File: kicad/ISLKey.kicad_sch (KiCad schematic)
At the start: 13 parts, among them J1 Exit Button N/O, J2 Door Contact N/C, J4 Tamper N/C, J5 Fire volt-free N/C (series, o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, K1 2-Ch Relay Module, U1 ISLKey Controller (TTGO), U2 PC817 fire-link monitor -> GP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

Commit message: kicad: rebuild ISLKey TTGO carrier as a real, manufacturable design
Replace the box-symbol connectivity sketch with a proper KiCad 10 design
generated from gen/ scripts that embed genuine library symbols (correct
pin<->pad maps) with footprints assigned:

- Schematic (ISLKey.kicad_sch): 40 parts, ERC 0/0. TTGO T-Display carrier
  with dual onboard SANYOU-SRD relays (2N2222 drivers, flyback, green status
  LED across each coil), monitored fire link (PC817 + COM<->fire jumper),
  wide-input isolated PSU (5-60V AC/DC -> KBU bridge + fuse -> isolated 12V
  DC-DC module -> 12->5V buck), 12V lock/aux output, and 18650 battery
  passthrough. PGND/GND kept separate to preserve isolation.
- PCB (ISLKey.kicad_pcb): all 40 footprints placed + nets assigned via
  pcbnew, board outline + 4x M3 holes, DRC 0 (only unrouted ratsnest).
- BOM (ISLKey-BOM.csv): 30 grouped line items, all real footprints.
- Generators: gen/kicad_lib.py, gen/make_schematic.py, gen/make_pcb.py.

Co-Authored-By: Claude Opus 4.8 <noreply@anthropic.com>
Claude-Session: https://claude.ai/code/session_01WaJbCVpNNC7xF4fkqWpjpA
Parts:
- removed BT1: 2x18650 UPS 5V, symbol islkey:UPS_18650
- removed D1: 1N4007 flyback, symbol islkey:Diode_1N4007
- removed J1: Exit Button N/O, symbol islkey:Conn_Exit
- removed J2: Door Contact N/C, symbol islkey:Conn_Door
- removed J4: Tamper N/C, symbol islkey:Conn_Tamper
- removed J5: Fire volt-free N/C (series, opens on fire), symbol islkey:Fire_Contact
- removed K1: 2-Ch Relay Module, symbol islkey:Relay_2Ch
- removed LK1: Electric Strike / Maglock 12V, symbol islkey:Lock
- removed PS1: 5V Mains PSU, symbol islkey:Mains_PSU
- removed PS2: 12V Lock PSU, symbol islkey:Lock_PSU
- removed R1: 2k2 opto LED series, symbol islkey:R_Opto
- removed U1: ISLKey Controller (TTGO), symbol islkey:ESP32_TTGO
- removed U2: PC817 fire-link monitor -> GPIO26, symbol islkey:Opto_PC817
- added BR1: KBU4M (4A), Diode_THT:Diode_Bridge_Vishay_KBU, symbol Diode_Bridge:KBU4A
- added C1: 100uF/16V, Capacitor_THT:CP_Radial_D6.3mm_P2.50mm, symbol Device:C_Polarized
- added C2, C3: 100nF, Capacitor_THT:C_Disc_D5.0mm_W2.5mm_P5.00mm, symbol Device:C
- added C4: 100uF/100V, Capacitor_THT:CP_Radial_D6.3mm_P2.50mm, symbol Device:C_Polarized
- added C5: 100uF/25V, Capacitor_THT:CP_Radial_D6.3mm_P2.50mm, symbol Device:C_Polarized
- added D1, D2: 1N4007, Diode_THT:D_DO-41_SOD81_P10.16mm_Horizontal, symbol Device:D
- added D3: PWR, LED_THT:LED_D3.0mm, symbol Device:LED
- added D4, D5: GRN, LED_THT:LED_D3.0mm, symbol Device:LED
- added F1: T2A, Fuse:Fuseholder_Clip-5x20mm_Keystone_3512_Inline_P23.62x7.27mm_D1.02x1.57mm_Horizontal, symbol Device:Fuse
- added J1: TTGO Left, Connector_PinSocket_2.54mm:PinSocket_1x12_P2.54mm_Vertical, symbol Connector_Generic:Conn_01x12
- added J10: 5-60V AC/DC IN, TerminalBlock_Phoenix:TerminalBlock_Phoenix_MKDS-3-2-5.08_1x02_P5.08mm_Horizontal, symbol Connector:Screw_Terminal_01x02
- added J11: 12V OUT (lock/aux), TerminalBlock_Phoenix:TerminalBlock_Phoenix_MKDS-3-2-5.08_1x02_P5.08mm_Horizontal, symbol Connector:Screw_Terminal_01x02
- added J13: TTGO batt pads, Connector_PinHeader_2.54mm:PinHeader_1x02_P2.54mm_Vertical, symbol Connector_Generic:Conn_01x02
- added J14: 18650 pack, TerminalBlock_Phoenix:TerminalBlock_Phoenix_MKDS-1,5-2-5.08_1x02_P5.08mm_Horizontal, symbol Connector:Screw_Terminal_01x02
- added J2: TTGO Right, Connector_PinSocket_2.54mm:PinSocket_1x12_P2.54mm_Vertical, symbol Connector_Generic:Conn_01x12
- added J3: Exit btn, TerminalBlock_Phoenix:TerminalBlock_Phoenix_MKDS-1,5-2-5.08_1x02_P5.08mm_Horizontal, symbol Connector:Screw_Terminal_01x02
- added J4: Door contact, TerminalBlock_Phoenix:TerminalBlock_Phoenix_MKDS-1,5-2-5.08_1x02_P5.08mm_Horizontal, symbol Connector:Screw_Terminal_01x02
- added J5: Tamper, TerminalBlock_Phoenix:TerminalBlock_Phoenix_MKDS-1,5-2-5.08_1x02_P5.08mm_Horizontal, symbol Connector:Screw_Terminal_01x02
- added J6: LOCK COM/NO/NC, TerminalBlock_Phoenix:TerminalBlock_Phoenix_MKDS-1,5-3-5.08_1x03_P5.08mm_Horizontal, symbol Connector:Screw_Terminal_01x03
- added J7: AUX COM/NO/NC, TerminalBlock_Phoenix:TerminalBlock_Phoenix_MKDS-1,5-3-5.08_1x03_P5.08mm_Horizontal, symbol Connector:Screw_Terminal_01x03
- added J8: Fire volt-free, TerminalBlock_Phoenix:TerminalBlock_Phoenix_MKDS-1,5-2-5.08_1x02_P5.08mm_Horizontal, symbol Connector:Screw_Terminal_01x02
- added J9: Fire link COM-Fire, Connector_PinHeader_2.54mm:PinHeader_1x02_P2.54mm_Vertical, symbol Connector_Generic:Conn_01x02
- added K1, K2: SRD-05VDC-SL-C, Relay_THT:Relay_SPDT_SANYOU_SRD_Series_Form_C, symbol Relay:SANYOU_SRD_Form_C
- added Q1, Q2: PN2222A, Package_TO_SOT_THT:TO-92_Inline, symbol Transistor_BJT:Q_NPN_EBC
- added R1, R3, R6, R7, R8: 1k, Resistor_THT:R_Axial_DIN0207_L6.3mm_D2.5mm_P7.62mm_Horizontal, symbol Device:R
- added R2, R4: 10k, Resistor_THT:R_Axial_DIN0207_L6.3mm_D2.5mm_P7.62mm_Horizontal, symbol Device:R
- added R5: 2k2, Resistor_THT:R_Axial_DIN0207_L6.3mm_D2.5mm_P7.62mm_Horizontal, symbol Device:R
- added U1: PC817, Package_DIP:DIP-4_W7.62mm, symbol Isolator:PC817
- added U3: ISO DCDC ->12V (e.g. Mornsun URB), Connector_PinHeader_2.54mm:PinHeader_1x04_P2.54mm_Vertical, symbol Connector_Generic:Conn_01x04
- added U4: BUCK 12->5V (e.g. MP1584), Connector_PinHeader_2.54mm:PinHeader_1x03_P2.54mm_Vertical, symbol Connector_Generic:Conn_01x03
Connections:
- net +12V: now also C5.1, J11.1 (Pin_1), U3.4 (Pin_4), U4.1 (Pin_1)
- net +5V: now also C1.1, C2.1, D1.1 (K), D2.1 (K), D3.2 (A), D4.2 (A), D5.2 (A), J2.12 (Pin_12), K1.5, K2.5, U4.3 (Pin_3)
- net DOOR: now also J2.8 (Pin_8), J4.1 (Pin_1)
- net EXIT: now also J1.8 (Pin_8), J3.1 (Pin_1)
- net FIRE_A: now also J8.1 (Pin_1), J9.2 (Pin_2), R5.1
- net GND: now also C1.2, C2.2, C3.2, C5.2, J1.1 (Pin_1), J1.10 (Pin_10), J1.11 (Pin_11), J1.2 (Pin_2), J11.2 (Pin_2), J2.11 (Pin_11), J3.2 (Pin_2), J4.2 (Pin_2), J5.2 (Pin_2), Q1.1 (E), Q2.1 (E), R2.2, R4.2, R6.2, U1.3, U3.3 (Pin_3), U4.2 (Pin_2)
- net OPTO_A: now also R5.2, U1.1
- net TAMPER: now also J2.10 (Pin_10), J5.1 (Pin_1)
- new net +3V3: C3.1, J1.12 (Pin_12), J2.1 (Pin_1)
- new net ACIN1: BR1.2, F1.2
- new net ACL: F1.1, J10.1 (Pin_1)
- new net ACN: BR1.3, J10.2 (Pin_2)
- new net D3K: D3.1 (K), R6.1
- new net D4K: D4.1 (K), R7.1
- new net D5K: D5.1 (K), R8.1
- new net FIRE_B: J8.2 (Pin_2), U1.2
- new net FIRE_SENSE: J2.9 (Pin_9), U1.4
- new net GND_BAT: J13.2 (Pin_2), J14.2 (Pin_2)
- new net K1_C: D1.2 (A), K1.2, Q1.3 (C), R7.2
- new net K2_C: D2.2 (A), K2.2, Q2.3 (C), R8.2
- new net LK1_COM: J6.1 (Pin_1), J9.1 (Pin_1), K1.1
- new net LK1_NC: J6.3 (Pin_3), K1.4
- new net LK1_NO: J6.2 (Pin_2), K1.3
- new net LK2_COM: J7.1 (Pin_1), K2.1
- new net LK2_NC: J7.3 (Pin_3), K2.4
- new net LK2_NO: J7.2 (Pin_2), K2.3
- new net PGND: BR1.4 (-), C4.2, U3.2 (Pin_2)
- new net RAWP: BR1.1 (+), C4.1, U3.1 (Pin_1)
- new net RLY1: J2.6 (Pin_6), R1.1
- new net RLY1_B: Q1.2 (B), R1.2, R2.1
- new net RLY2: J2.7 (Pin_7), R3.1
- new net RLY2_B: Q2.2 (B), R3.2, R4.1
- new net VBAT: J13.1 (Pin_1), J14.1 (Pin_1)
- no-connect marks 0 -> 10
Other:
- title: ISLKey Door Controller — TTGO T-Display -> ISLKey TTGO Carrier Board

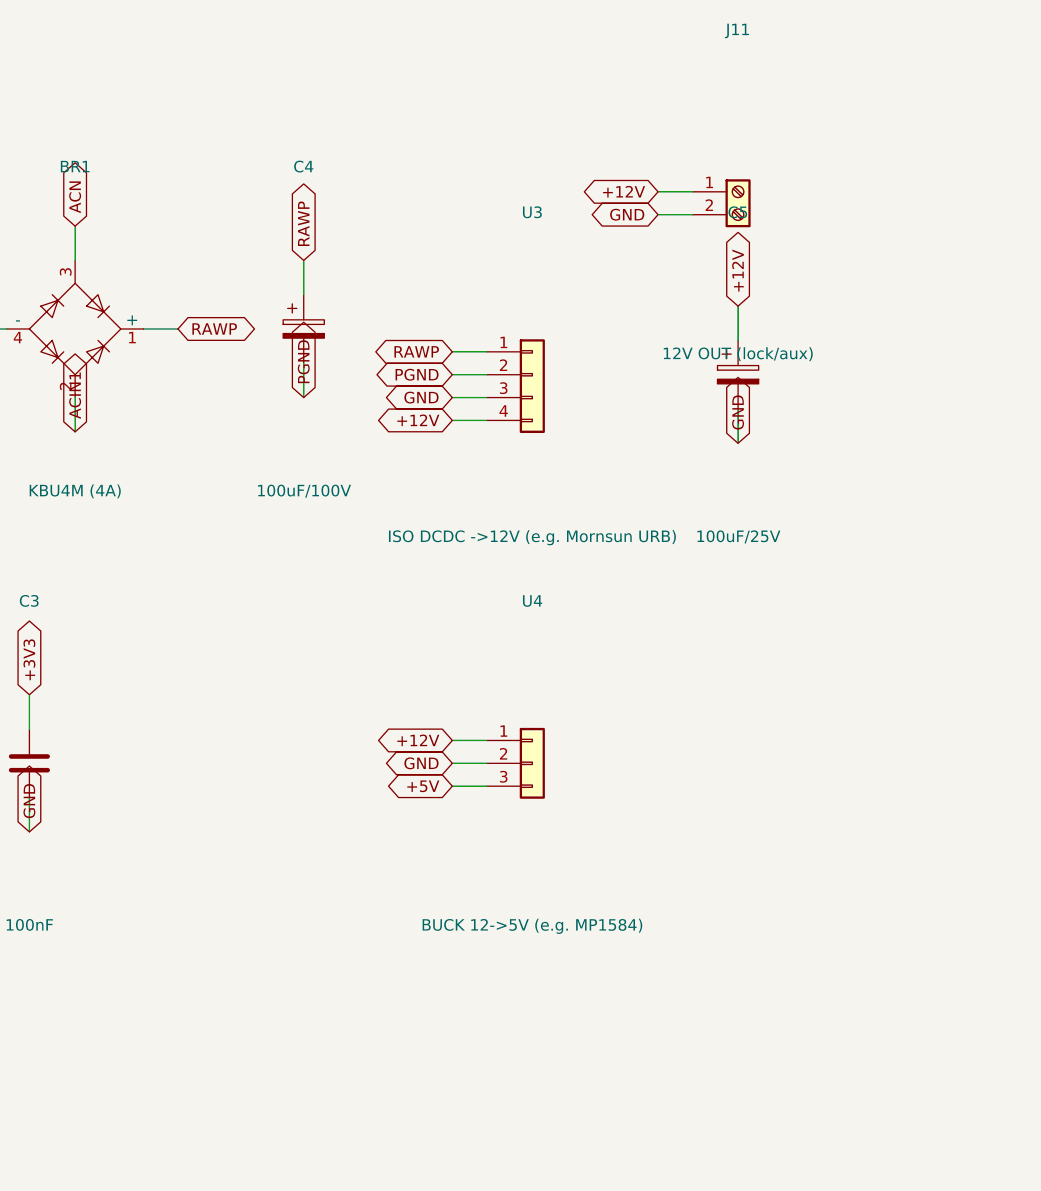
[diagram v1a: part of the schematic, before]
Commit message: kicad: use real Traco parts for the wide-input PSU
Replace the two generic module-header placeholders with genuine parts +
KiCad footprints:
- U3 isolated 12V: Traco TEN20-2412WIN (9-36V in -> isolated 12V/20W),
  footprint Converter_DCDC_TRACO_TEN20-xxxx_THT. Remote pin left open
  (positive logic, open = ON); Trim pin NC.
- U4 buck 12->5V for the TTGO: Traco TSR-1-2450 (SIP-3), footprint
  Converter_DCDC_TRACO_TSR-1_THT.
- Add PWR_FLAG on the raw primary rails (RAWP/PGND) so ERC sees them driven
  (bridge diode outputs are 'passive'); flags excluded from board + BOM.

ERC 0/0, DRC 0 (unrouted ratsnest only). One board covers 12/24V systems;
pin-compatible TEN20-4812WIN swaps in for 48V.

Co-Authored-By: Claude Opus 4.8 <noreply@anthropic.com>
Claude-Session: https://claude.ai/code/session_01WaJbCVpNNC7xF4fkqWpjpA
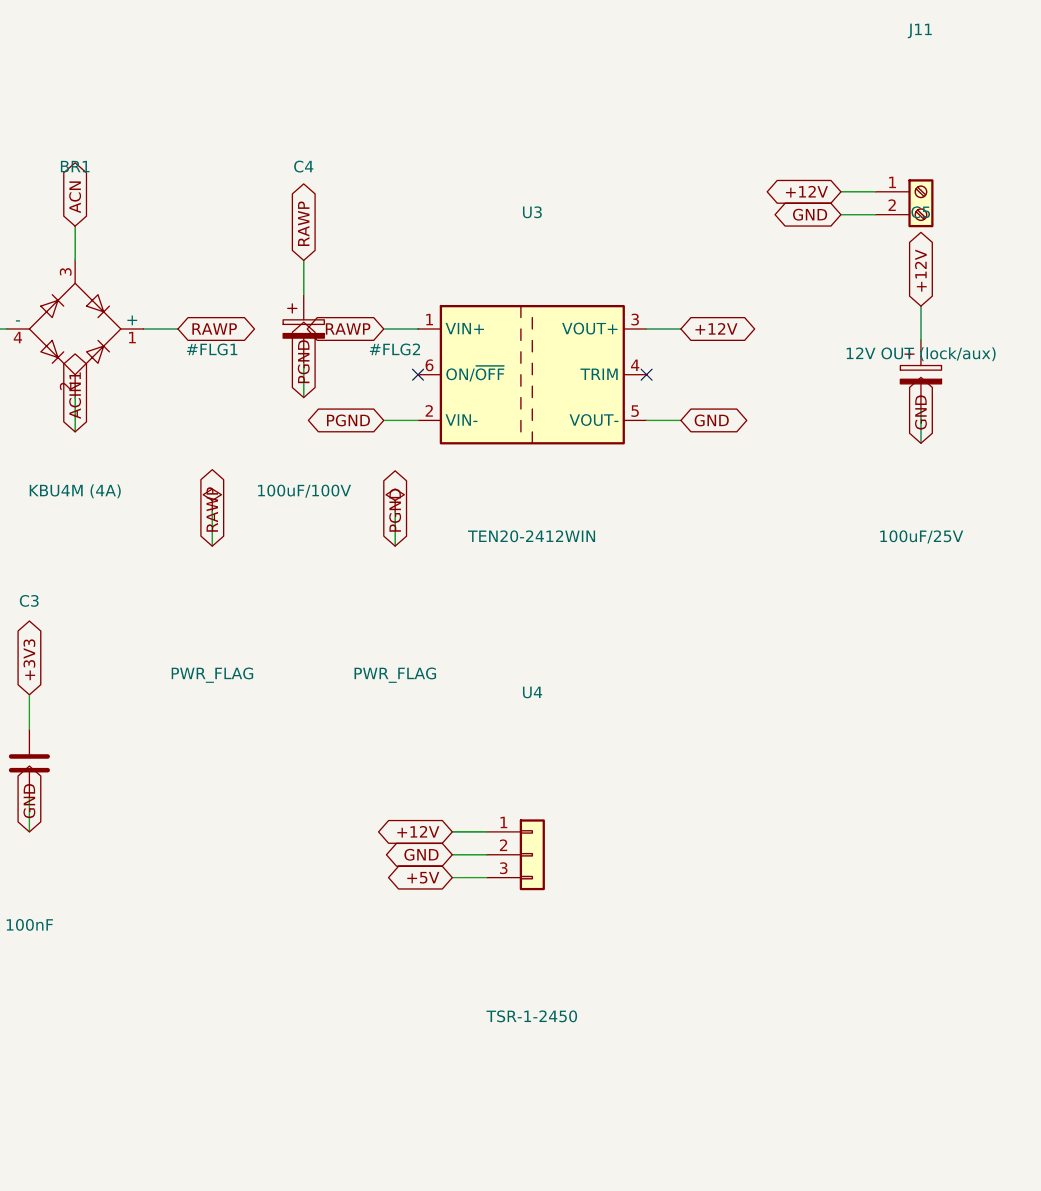
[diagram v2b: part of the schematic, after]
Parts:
- removed U3: ISO DCDC ->12V (e.g. Mornsun URB), Connector_PinHeader_2.54mm:PinHeader_1x04_P2.54mm_Vertical, symbol Connector_Generic:Conn_01x04
- added U3: TEN20-2412WIN, Converter_DCDC:Converter_DCDC_TRACO_TEN20-xxxx_THT, symbol Converter_DCDC:TEN20-2411WIN
- U4: value BUCK 12->5V (e.g. MP1584) -> TSR-1-2450; footprint Connector_PinHeader_2.54mm:PinHeader_1x03_P2.54mm_Vertical -> Converter_DCDC:Converter_DCDC_TRACO_TSR-1_THT
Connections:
- net +12V: now also U3.3 (VOUT+)
- net GND: now also U3.5 (VOUT-)
- net PGND: now also U3.2 (VIN-)
- net RAWP: now also U3.1 (VIN+)
- no-connect marks 10 -> 12

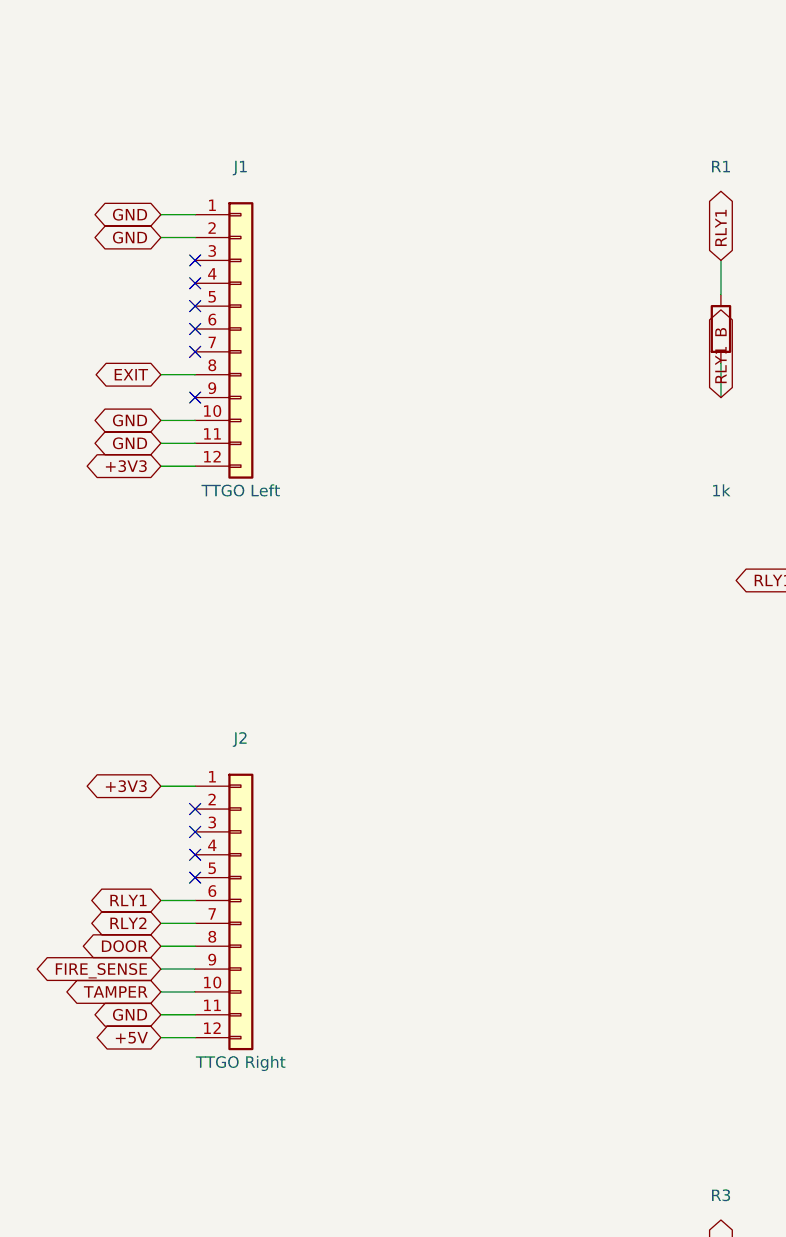
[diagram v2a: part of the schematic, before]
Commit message: kicad: real TTGO T-Display footprint + routing-aware placement
- Replace the two guessed 1x12 header sockets with a single correct TTGO
  T-Display module footprint + symbol (from GillesOdb/ttgo-tdisplay-kicad,
  legacy .kicad_mod + .lib converted to KiCad 10). Confirms the 22.86mm
  header row spacing. Pad<->GPIO verified against the module pinout
  (pad7=GPIO32, 6=GPIO33, 5=GPIO25, 4=GPIO26, 3=GPIO27, 20=GPIO13,
  1=5V, 2/13/14/22/23=GND, 12/24=3V3); symbol pins retyped passive.
- Local libs: lib/ISLKey.pretty + lib/ISLKey.kicad_sym, with project
  fp-lib-table / sym-lib-table so KiCad resolves them.
- make_pcb.py: routing-aware floorplan (inputs on left edge, TTGO centre,
  each relay driver->coil->contacts->terminal in line, fire monitor row,
  power chain along the bottom with the U3 isolation barrier splitting
  primary/secondary). Power row auto-spaced by real footprint width.

ERC 0/0. DRC: no physical collisions (only cosmetic silk/text-height from
the imported footprint's 0.75mm silk). Board ~185x164mm, ratsnest ready.

Co-Authored-By: Claude Opus 4.8 <noreply@anthropic.com>
Claude-Session: https://claude.ai/code/session_01WaJbCVpNNC7xF4fkqWpjpA
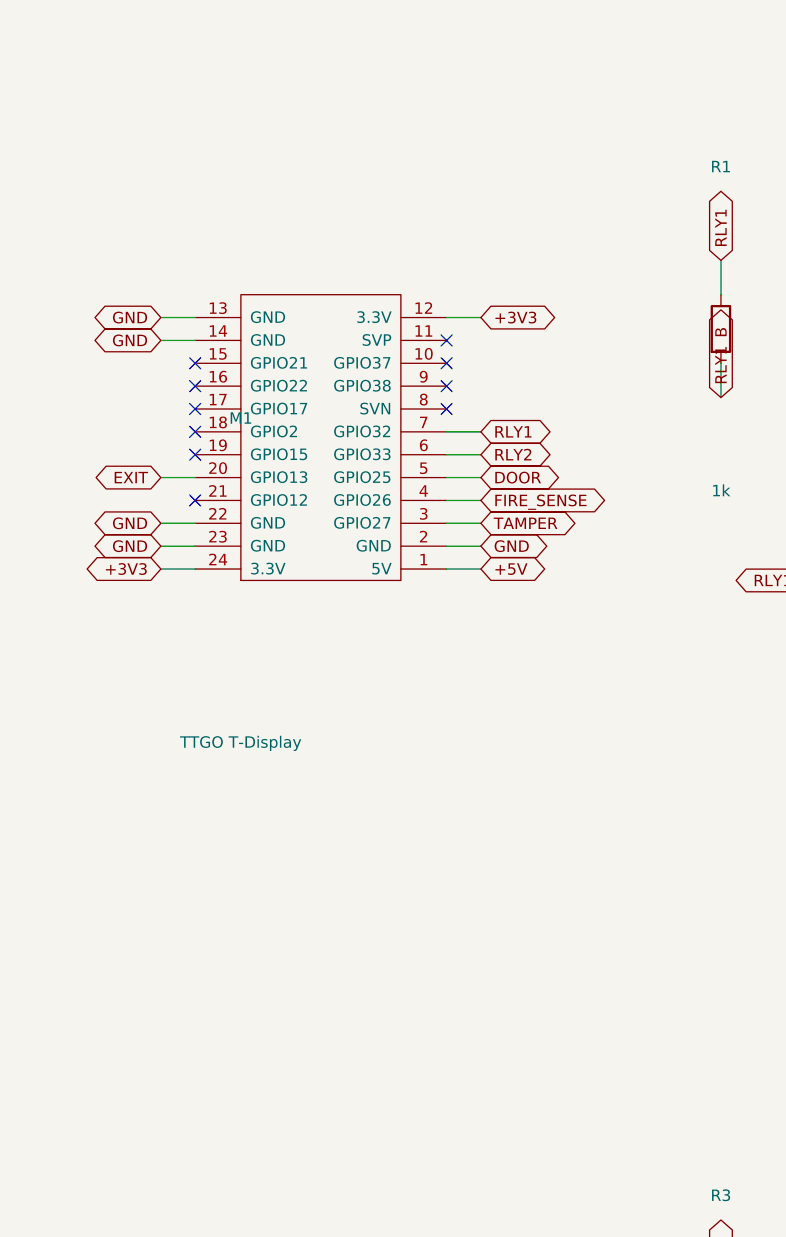
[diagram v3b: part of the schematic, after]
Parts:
- removed J1: TTGO Left, Connector_PinSocket_2.54mm:PinSocket_1x12_P2.54mm_Vertical, symbol Connector_Generic:Conn_01x12
- removed J2: TTGO Right, Connector_PinSocket_2.54mm:PinSocket_1x12_P2.54mm_Vertical, symbol Connector_Generic:Conn_01x12
- added M1: TTGO T-Display, ISLKey:TTGO_ESP32_TDisplay_v1.1, symbol ISLKey:TTGO_ESP32_TDISPLAY_V1.1
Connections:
- net +3V3: now also M1.12 (3.3V), M1.24 (3.3V)
- net +5V: now also M1.1 (5V)
- net DOOR: now also M1.5 (GPIO25)
- net EXIT: now also M1.20 (GPIO13)
- net FIRE_SENSE: now also M1.4 (GPIO26)
- net GND: now also M1.13 (GND), M1.14 (GND), M1.2 (GND), M1.22 (GND), M1.23 (GND)
- net RLY1: now also M1.7 (GPIO32)
- net RLY2: now also M1.6 (GPIO33)
- net TAMPER: now also M1.3 (GPIO27)

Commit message: kicad: add RTC (DS3231), on-board 2x18650 holders, and ground pour
- RTC: DS3231M (I2C on GPIO21/22 via the TTGO's onboard pull-ups),
  CR2032-backed (Keystone 3002) + 100nF. PWR_FLAGs on +3V3/RTC_VBAT.
- Battery: two Keystone 1042 1x18650 holders in parallel (BT1/BT2) on
  VBAT/GND_BAT, replacing the external-holder terminal (J14 removed).
- Ground plane: GND-filled zones on F.Cu and B.Cu (fill done on a reloaded
  board -- filling the freshly-built in-memory board segfaults pcbnew).

ERC 0/0, DRC no physical collisions (cosmetic silk/text-height only).
Board grows to ~219x200mm from the 18650 holders.

Co-Authored-By: Claude Opus 4.8 <noreply@anthropic.com>
Claude-Session: https://claude.ai/code/session_01WaJbCVpNNC7xF4fkqWpjpA
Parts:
- removed J14: 18650 pack, TerminalBlock_Phoenix:TerminalBlock_Phoenix_MKDS-1,5-2-5.08_1x02_P5.08mm_Horizontal, symbol Connector:Screw_Terminal_01x02
- added BT1, BT2: 18650, Battery:BatteryHolder_Keystone_1042_1x18650, symbol Device:Battery
- added BT3: CR2032, Battery:BatteryHolder_Keystone_3002_1x2032, symbol Device:Battery_Cell
- added C6: 100nF, Capacitor_THT:C_Disc_D5.0mm_W2.5mm_P5.00mm, symbol Device:C
- added U5: DS3231M, Package_SO:SOIC-16W_7.5x10.3mm_P1.27mm, symbol Timer_RTC:DS3231M
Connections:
- net +3V3: now also C6.1, U5.2 (VCC)
- net GND: now also BT3.2 (-), C6.2, U5.10 (GND), U5.11 (GND), U5.12 (GND), U5.13 (GND), U5.5 (GND), U5.6 (GND), U5.7 (GND), U5.8 (GND), U5.9 (GND)
- net GND_BAT: now also BT1.2 (-), BT2.2 (-)
- net VBAT: now also BT1.1 (+), BT2.1 (+)
- net I2C_SDA: now reaches M1.15 (GPIO21)
- net I2C_SDA: now also U5.15 (SDA)
- net I2C_SCL: now reaches M1.16 (GPIO22)
- net I2C_SCL: now also U5.16 (SCL)
- new net RTC_VBAT: BT3.1 (+), U5.14 (VBAT)
- no-connect marks 12 -> 13
